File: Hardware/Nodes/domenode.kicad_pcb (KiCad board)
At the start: 2 copper layers, 100 x 70 mm, 89 parts, among them J1 MIC_JUMPER, J10 5V, J11 TOUCH, J12 24V, J13 CAN_BOARD, J15 RGB_SHIELD, J16 RGB_SHIELD, J17 GROVE/I2C, J18 ISP, J19 CAN_IN, J2 MIC_HEADER, J20 CAN_OUT, J21 SWITCHES, J3 SW0, J4 CANTERM, J5 3V3, J6 POWER_TEST, J9 SENSOR, Q1 MMBT918 (2N706 equiv), Q2 MMBT2222A (2N2222 equiv), SW1 SW1, SW2 SW2, SW3 RESET, SW4 BOOT, U1 MINI-360, U2 AMS1117-3.3, U3 ESP32-WROOM, U5 TSDP341xx, U6 SN65HVD230

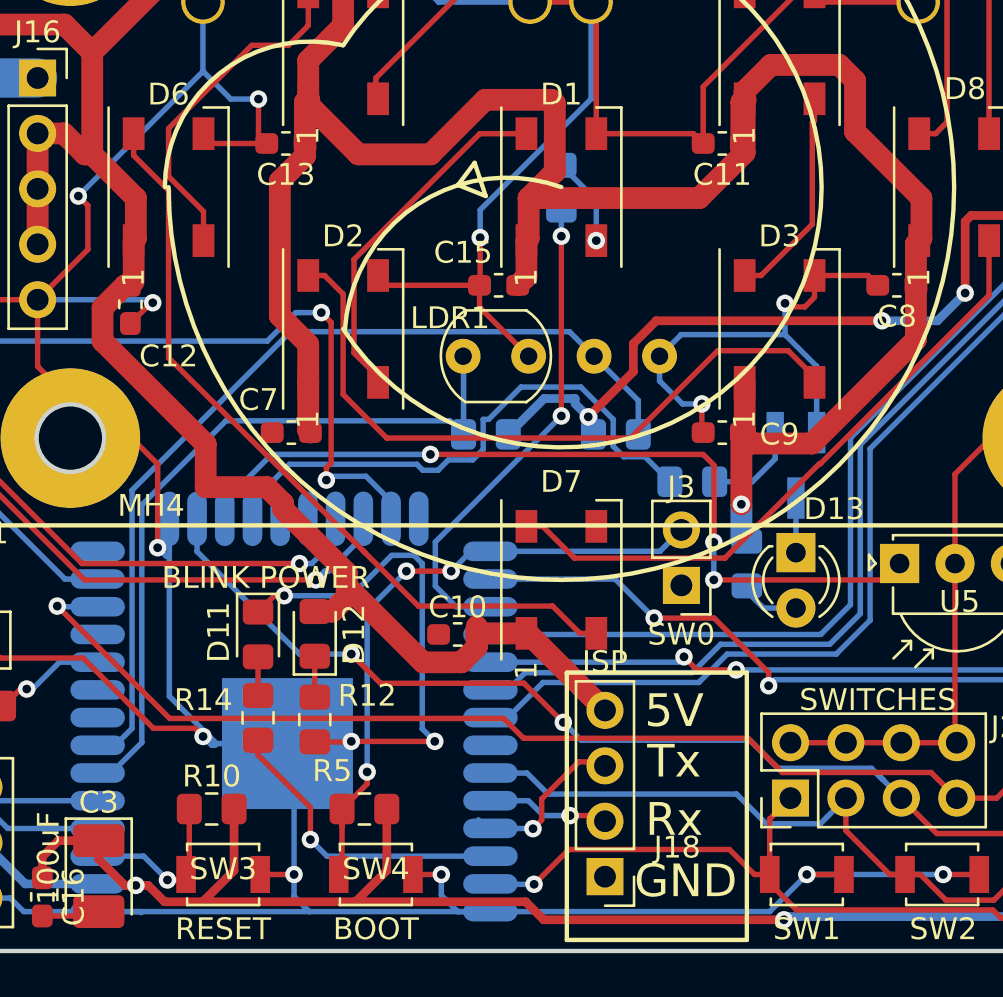
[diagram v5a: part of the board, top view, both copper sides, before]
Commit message: First clean DRC done.
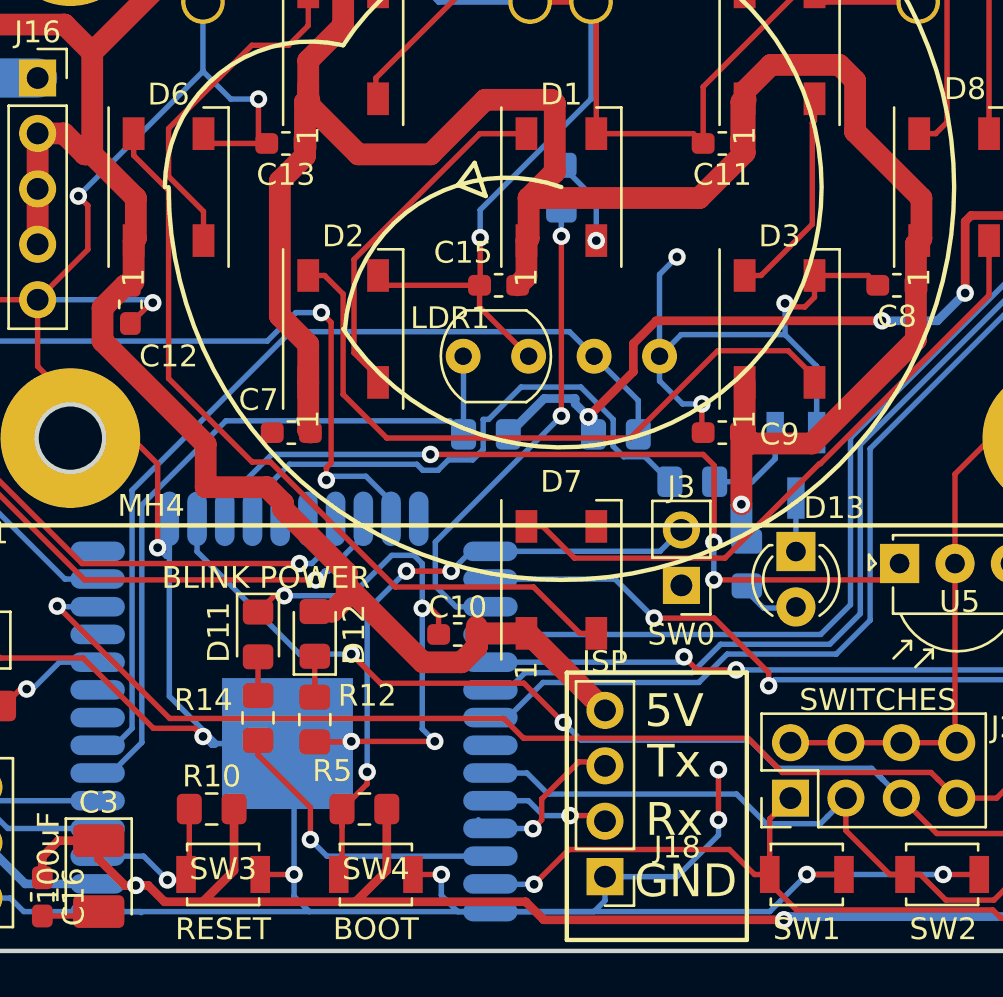
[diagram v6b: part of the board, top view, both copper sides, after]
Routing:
- net CANGND: track 510.3 -> 532.4 mm, vias 17 -> 21
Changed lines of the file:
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@@
     (thickness 1.6)
     (drawings 59)
-    (tracks 942)
+    (tracks 960)
     (zones 0)
     (modules 89)
@@
   )
   (module LED_THT:LED_D3.0mm_IRBlack (layer F.Cu)
-    (at 159.25 121.75 270)
+    (at 159.25 121.7 270)
     (descr "IR-ED, diameter 3.0mm, 2 pins, color: black")
     (tags "IR infrared LED diameter 3.0mm 2 pins black")
@@
   (via (at 159.75 136.5) (size 0.8) (drill 0.4) (layers F.Cu B.Cu) (net 4))
   (segment (start 159.75 136.5) (end 161.45 136.5) (width 0.25) (layer F.Cu) (net 4) (status 20))
-  (segment (start 158.05 138.2) (end 159.75 136.5) (width 0.25) (layer B.Cu) (net 4))
-  (segment (start 145.25 138.2) (end 158.05 138.2) (width 0.25) (layer B.Cu) (net 4) (status 10))
   (segment (start 143.75 138.2) (end 143 137.45) (width 0.25) (layer B.Cu) (net 4))
   (segment (start 145.25 138.2) (end 143.75 138.2) (width 0.25) (layer B.Cu) (net 4) (status 10))
@@
   (segment (start 138.875 130.4) (end 142.7 130.4) (width 0.25) (layer F.Cu) (net 4))
   (via (at 142.7 130.4) (size 0.8) (drill 0.4) (layers F.Cu B.Cu) (net 4))
-  (segment (start 142.125001 129.825001) (end 142.125001 122.251999) (width 0.25) (layer B.Cu) (net 4))
   (segment (start 142.7 130.4) (end 142.125001 129.825001) (width 0.25) (layer B.Cu) (net 4))
   (segment (start 141.748001 121.874999) (end 140.725001 121.874999) (width 0.25) (layer B.Cu) (net 4))
@@
   (segment (start 126.108491 114.506284) (end 125.556415 114.593723) (width 0.25) (layer F.Cu) (net 4) (status 30))
   (segment (start 126.817398 114.506284) (end 126.108491 114.506284) (width 0.25) (layer F.Cu) (net 4) (status 30))
-  (segment (start 130.00002 117.688906) (end 126.817398 114.506284) (width 0.25) (layer F.Cu) (net 4) (status 20))
   (segment (start 130.00002 121.525) (end 130.00002 117.688906) (width 0.25) (layer F.Cu) (net 4))
   (segment (start 114.54 105.17) (end 114.54 104.48) (width 0.25) (layer F.Cu) (net 4) (status 30))
@@
   (segment (start 126.8 105.845) (end 126.365 105.41) (width 0.25) (layer F.Cu) (net 4))
   (segment (start 126.8 107.86) (end 126.8 105.845) (width 0.25) (layer F.Cu) (net 4))
+  (segment (start 130.00002 117.688906) (end 126.817398 114.506284) (width 0.25) (layer F.Cu) (net 4) (status 20))
+  (segment (start 158.05 138.2) (end 159.75 136.5) (width 0.25) (layer B.Cu) (net 4))
+  (segment (start 145.25 138.2) (end 158.05 138.2) (width 0.25) (layer B.Cu) (net 4))
+  (segment (start 150.5 137.7) (end 150.5 136.6) (width 0.25) (layer B.Cu) (net 4))
+  (segment (start 150 138.2) (end 150.5 137.7) (width 0.25) (layer B.Cu) (net 4))
+  (segment (start 145.25 138.2) (end 150 138.2) (width 0.25) (layer B.Cu) (net 4))
+  (via (at 153.8 108.2) (size 0.8) (drill 0.4) (layers F.Cu B.Cu) (net 4))
+  (segment (start 153 112.75) (end 153 109) (width 0.25) (layer B.Cu) (net 4))
+  (segment (start 153 109) (end 153.8 108.2) (width 0.25) (layer B.Cu) (net 4))
+  (segment (start 150.5 136.6) (end 153.8 136.6) (width 0.25) (layer B.Cu) (net 4))
+  (segment (start 153.8 136.6) (end 155.7 134.7) (width 0.25) (layer B.Cu) (net 4))
+  (via (at 155.7 134) (size 0.8) (drill 0.4) (layers F.Cu B.Cu) (net 4))
+  (segment (start 155.7 134.7) (end 155.7 134) (width 0.25) (layer B.Cu) (net 4))
+  (segment (start 155.7 134) (end 155.7 133.434315) (width 0.25) (layer F.Cu) (net 4))
+  (via (at 155.7 131.7) (size 0.8) (drill 0.4) (layers F.Cu B.Cu) (net 4))
+  (segment (start 155.7 133.434315) (end 155.7 131.7) (width 0.25) (layer F.Cu) (net 4))
+  (segment (start 142.875 125.5) (end 142.875 124.675) (width 0.25) (layer F.Cu) (net 4))
+  (via (at 142.125001 124.3) (size 0.8) (drill 0.4) (layers F.Cu B.Cu) (net 4))
+  (segment (start 142.5 124.3) (end 142.125001 124.3) (width 0.25) (layer F.Cu) (net 4))
+  (segment (start 142.875 124.675) (end 142.5 124.3) (width 0.25) (layer F.Cu) (net 4))
+  (segment (start 142.125001 129.825001) (end 142.125001 124.3) (width 0.25) (layer B.Cu) (net 4))
+  (segment (start 142.125001 124.3) (end 142.125001 122.251999) (width 0.25) (layer B.Cu) (net 4))
   (segment (start 113.5 90.1) (end 113.5 85.2) (width 0.4) (layer F.Cu) (net 5) (status 20))
   (segment (start 112.19 88.79) (end 106.25 88.79) (width 0.4) (layer F.Cu) (net 5) (status 20))
@@
   (segment (start 136.9 97.6) (end 136 98.5) (width 0.25) (layer F.Cu) (net 59))
   (segment (start 136.9 96.05) (end 136.9 97.6) (width 0.25) (layer F.Cu) (net 59) (status 10))
-  (segment (start 128.9 103.55) (end 128.9 102.55) (width 0.25) (layer F.Cu) (net 60) (status 20))
-  (segment (start 130.5 112.82051) (end 130.5 105.15) (width 0.25) (layer F.Cu) (net 60))
-  (segment (start 130.5 105.15) (end 128.9 103.55) (width 0.25) (layer F.Cu) (net 60))
-  (segment (start 149.35 125.45) (end 148.1 124.2) (width 0.25) (layer F.Cu) (net 60))
-  (segment (start 150.1 125.45) (end 149.35 125.45) (width 0.25) (layer F.Cu) (net 60) (status 10))
-  (segment (start 141.949217 124.2) (end 139.4 121.650783) (width 0.25) (layer F.Cu) (net 60))
-  (segment (start 148.1 124.2) (end 141.949217 124.2) (width 0.25) (layer F.Cu) (net 60))
-  (segment (start 139.5 121.75) (end 139.4 121.650783) (width 0.25) (layer F.Cu) (net 60))
-  (segment (start 139.4 121.650783) (end 130.5 112.82051) (width 0.25) (layer F.Cu) (net 60))
+  (segment (start 149.35 125.45) (end 150.1 125.45) (width 0.25) (layer F.Cu) (net 60))
+  (segment (start 147.225001 123.325001) (end 149.35 125.45) (width 0.25) (layer F.Cu) (net 60))
+  (segment (start 128.9 102.55) (end 128.9 103.55) (width 0.25) (layer F.Cu) (net 60))
+  (segment (start 128.9 103.55) (end 130.5 105.15) (width 0.25) (layer F.Cu) (net 60))
+  (segment (start 130.5 105.15) (end 130.5 113.771838) (width 0.25) (layer F.Cu) (net 60))
+  (segment (start 130.5 113.771838) (end 134.328162 117.6) (width 0.25) (layer F.Cu) (net 60))
+  (segment (start 134.328162 117.6) (end 135.168103 117.6) (width 0.25) (layer F.Cu) (net 60))
+  (segment (start 140.893104 123.325001) (end 147.225001 123.325001) (width 0.25) (layer F.Cu) (net 60))
+  (segment (start 135.168103 117.6) (end 140.893104 123.325001) (width 0.25) (layer F.Cu) (net 60))
   (segment (start 168.1 107.45) (end 168.1 109.948163) (width 0.25) (layer F.Cu) (net 61) (status 10))
   (segment (start 168.1 109.948163) (end 160.374081 117.674082) (width 0.25) (layer F.Cu) (net 61))
@@
     (connect_pads (clearance 0.508))
     (min_thickness 0.254)
-    (fill (arc_segments 16) (thermal_gap 0.508) (thermal_bridge_width 0.508) (smoothing fillet))
+    (fill yes (arc_segments 16) (thermal_gap 0.508) (thermal_bridge_width 0.508) (smoothing fillet))
     (polygon
       (pts
@@
     (connect_pads (clearance 0.508))
     (min_thickness 0.254)
-    (fill (arc_segments 16) (thermal_gap 0.508) (thermal_bridge_width 0.508) (smoothing fillet))
+    (fill yes (arc_segments 16) (thermal_gap 0.508) (thermal_bridge_width 0.508) (smoothing fillet))
     (polygon
       (pts

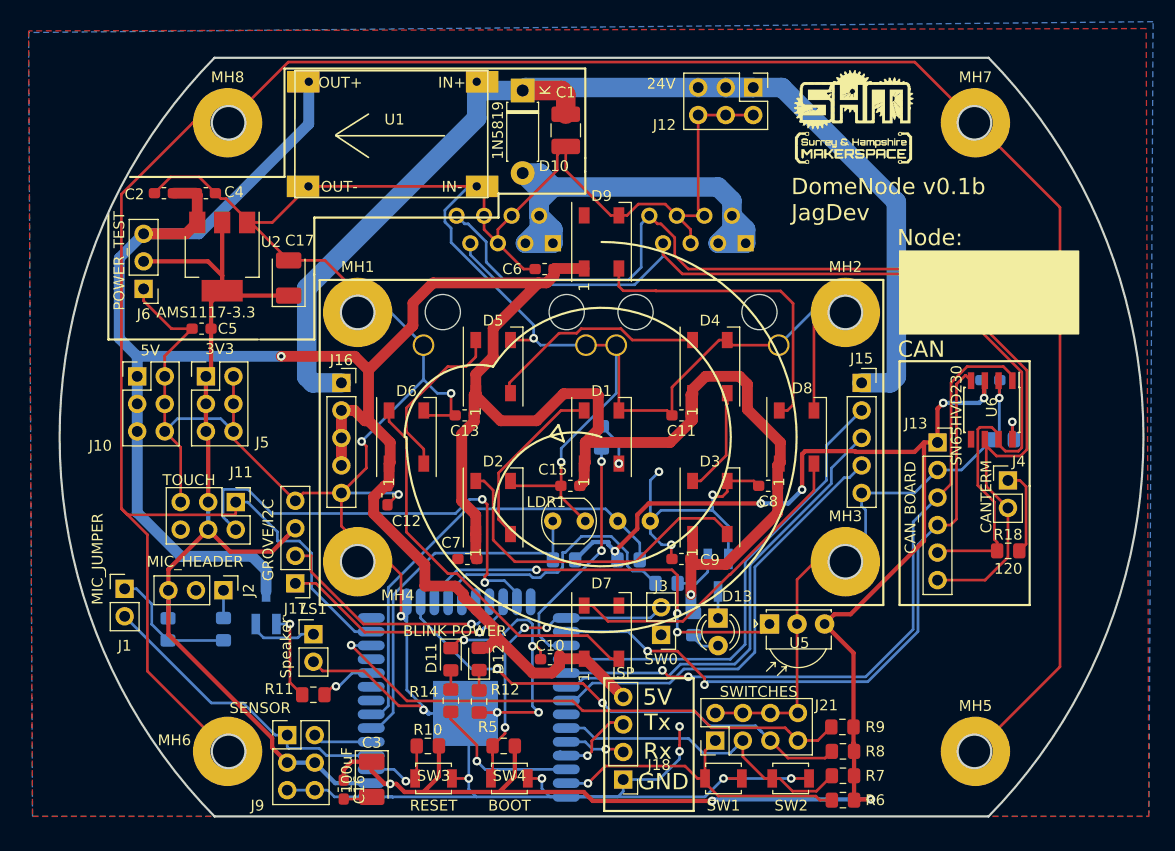
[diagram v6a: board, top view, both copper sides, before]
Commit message: Added ground vias for bald patches. Second clean DRC
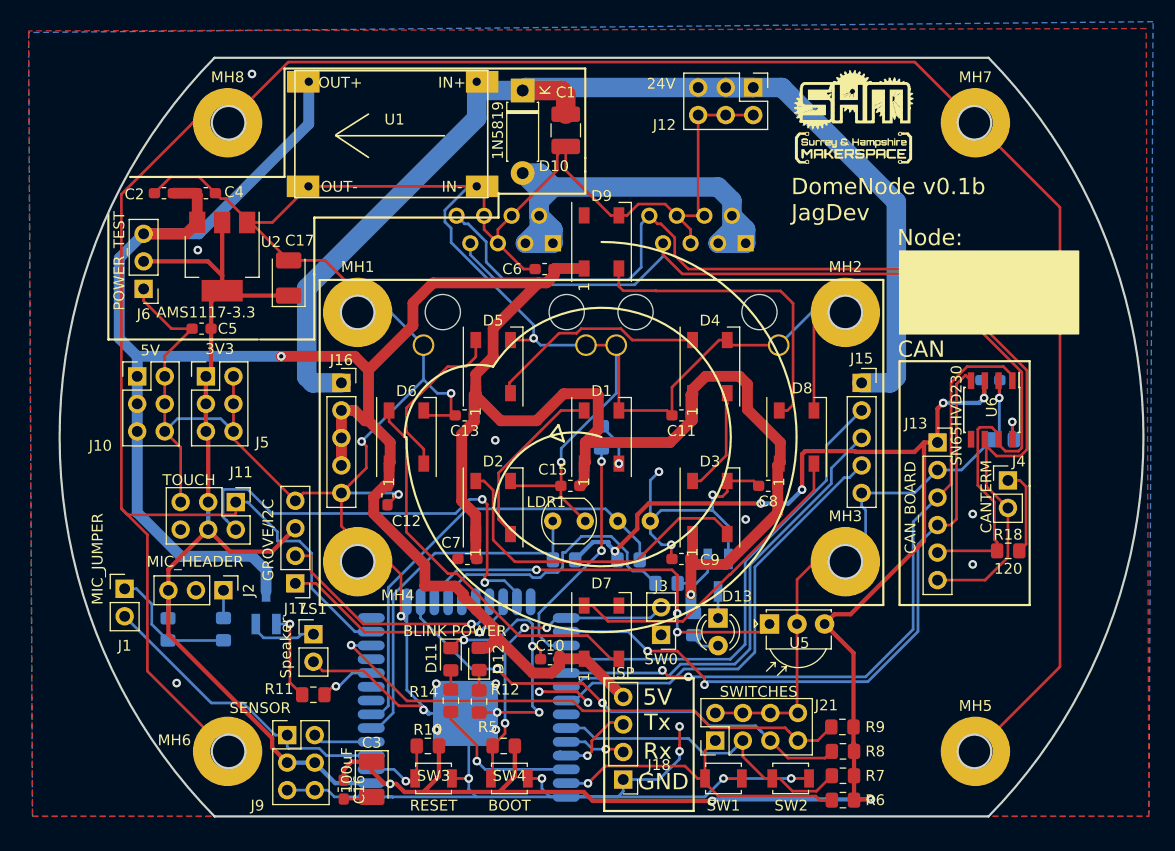
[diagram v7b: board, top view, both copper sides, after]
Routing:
- net CANGND: track 532.4 -> 537.4 mm, vias 21 -> 34
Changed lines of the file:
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@@
     (thickness 1.6)
     (drawings 59)
-    (tracks 960)
+    (tracks 976)
     (zones 0)
     (modules 89)
@@
   (gr_line (start 174.5 90.5) (end 122.5 90.5) (layer F.SilkS) (width 0.2))
   (gr_line (start 174.5 120.5) (end 174.5 90.5) (layer F.SilkS) (width 0.2))
+  (via (at 133.25 132) (size 0.8) (drill 0.4) (layers F.Cu B.Cu) (net 4))
+  (via (at 138.75 132) (size 0.8) (drill 0.4) (layers F.Cu B.Cu) (net 4))
+  (via (at 138.75 127.75) (size 0.8) (drill 0.4) (layers F.Cu B.Cu) (net 4))
+  (via (at 133.25 127.75) (size 0.8) (drill 0.4) (layers F.Cu B.Cu) (net 4))
   (segment (start 179.66 115.5) (end 179.5 115.66) (width 0.25) (layer F.Cu) (net 1) (status 30))
   (segment (start 185 115.5) (end 179.66 115.5) (width 0.25) (layer F.Cu) (net 1) (status 30))
@@
   (segment (start 138.875 130.4) (end 136.05 130.4) (width 0.25) (layer B.Cu) (net 4) (status 30))
   (segment (start 138.875 130.4) (end 142.7 130.4) (width 0.25) (layer F.Cu) (net 4))
-  (via (at 142.7 130.4) (size 0.8) (drill 0.4) (layers F.Cu B.Cu) (net 4))
+  (via (at 142.75 130.4) (size 0.8) (drill 0.4) (layers F.Cu B.Cu) (net 4))
   (segment (start 142.7 130.4) (end 142.125001 129.825001) (width 0.25) (layer B.Cu) (net 4))
   (segment (start 141.748001 121.874999) (end 140.725001 121.874999) (width 0.25) (layer B.Cu) (net 4))
@@
   (segment (start 142.125001 129.825001) (end 142.125001 124.3) (width 0.25) (layer B.Cu) (net 4))
   (segment (start 142.125001 124.3) (end 142.125001 122.251999) (width 0.25) (layer B.Cu) (net 4))
+  (via (at 109.3 127.7) (size 0.8) (drill 0.4) (layers F.Cu B.Cu) (net 4))
+  (via (at 138.7 105.3) (size 0.8) (drill 0.4) (layers F.Cu B.Cu) (net 4))
+  (via (at 161.8 112.6) (size 0.8) (drill 0.4) (layers F.Cu B.Cu) (net 4))
+  (via (at 182.75 112.1) (size 0.8) (drill 0.4) (layers F.Cu B.Cu) (net 4))
+  (via (at 182.75 116.75) (size 0.8) (drill 0.4) (layers F.Cu B.Cu) (net 4))
+  (via (at 142.75 128.5) (size 0.8) (drill 0.4) (layers F.Cu B.Cu) (net 4))
+  (segment (start 142.75 128.5) (end 143.315685 128.5) (width 0.25) (layer F.Cu) (net 4))
+  (segment (start 143.315685 128.5) (end 146.25 128.5) (width 0.25) (layer F.Cu) (net 4))
+  (via (at 147.25 129.5) (size 0.8) (drill 0.4) (layers F.Cu B.Cu) (net 4))
+  (segment (start 146.25 128.5) (end 147.25 129.5) (width 0.25) (layer F.Cu) (net 4))
+  (via (at 116.25 71.5) (size 0.8) (drill 0.4) (layers F.Cu B.Cu) (net 4))
+  (via (at 111.25 87.75) (size 0.8) (drill 0.4) (layers F.Cu B.Cu) (net 4))
   (segment (start 113.5 90.1) (end 113.5 85.2) (width 0.4) (layer F.Cu) (net 5) (status 20))
   (segment (start 112.19 88.79) (end 106.25 88.79) (width 0.4) (layer F.Cu) (net 5) (status 20))
@@
   (via (at 141.4 122.6) (size 0.8) (drill 0.4) (layers F.Cu B.Cu) (net 11))
   (segment (start 143.44999 122.6) (end 141.4 122.6) (width 0.25) (layer F.Cu) (net 11))
-  (segment (start 141.4 122.6) (end 139.6 124.4) (width 0.25) (layer B.Cu) (net 11))
-  (via (at 139.6 131.8) (size 0.8) (drill 0.4) (layers F.Cu B.Cu) (net 11))
-  (segment (start 139.6 124.4) (end 139.6 131.8) (width 0.25) (layer B.Cu) (net 11))
-  (segment (start 139.6 132.35) (end 138.45 133.5) (width 0.25) (layer F.Cu) (net 11) (status 20))
-  (segment (start 139.6 131.8) (end 139.6 132.35) (width 0.25) (layer F.Cu) (net 11))
+  (via (at 139.6 131.4) (size 0.8) (drill 0.4) (layers F.Cu B.Cu) (net 11))
+  (segment (start 139.6 132.35) (end 138.45 133.5) (width 0.25) (layer F.Cu) (net 11))
+  (segment (start 139.6 131.4) (end 139.6 132.35) (width 0.25) (layer F.Cu) (net 11))
+  (segment (start 139.6 124.4) (end 141.4 122.6) (width 0.25) (layer B.Cu) (net 11))
+  (segment (start 139.6 131.4) (end 139.6 124.4) (width 0.25) (layer B.Cu) (net 11))
   (segment (start 140.695 119.4) (end 139.545 118.25) (width 0.25) (layer B.Cu) (net 12) (status 10))
   (segment (start 140.695 120.2) (end 140.695 119.4) (width 0.25) (layer B.Cu) (net 12) (status 30))
